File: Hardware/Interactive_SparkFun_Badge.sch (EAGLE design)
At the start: 30 parts, among them J1 AVR_SPI_PRG_6PTH, U1 ATMEGA328P

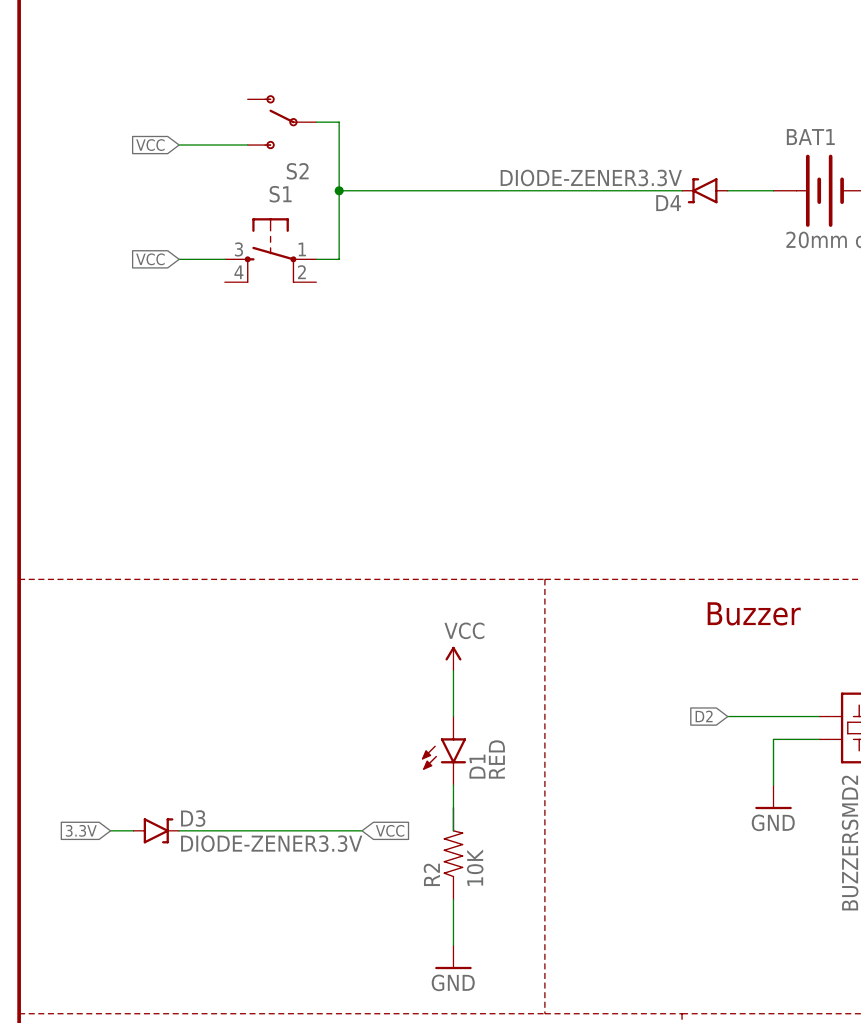
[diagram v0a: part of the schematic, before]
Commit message: Switching to Schottky diode
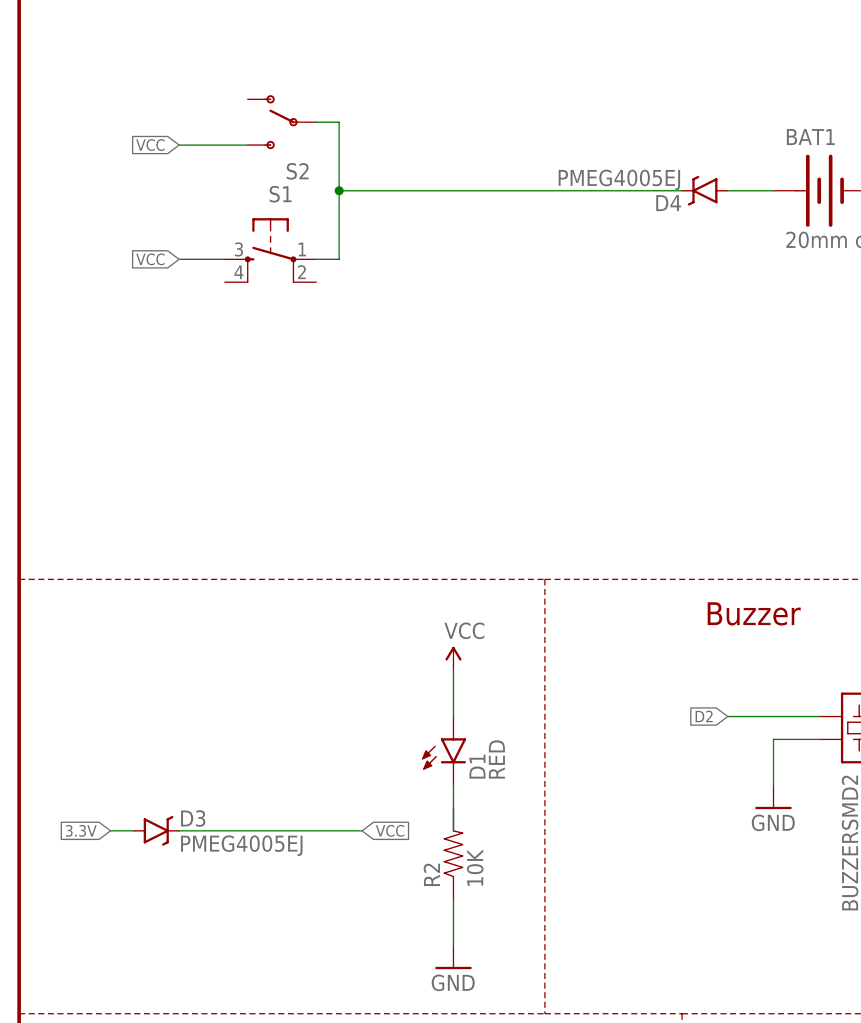
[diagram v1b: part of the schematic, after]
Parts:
- D3, D4: value DIODE-ZENER3.3V -> PMEG4005EJ; device SparkFun-DiscreteSemi:DIODE-ZENER3.3V -> SparkFun-DiscreteSemi:DIODE-SCHOTTKY-PMEG4005EJ
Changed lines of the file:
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@@
 <part name="J1" library="SparkFun-Connectors" deviceset="AVR_SPI_PRG_6" device="PTH" value="AVR_SPI_PRG_6PTH"/>
 <part name="U$3" library="ML8511" deviceset="ALPHABET" device=""/>
-<part name="D3" library="SparkFun-DiscreteSemi" deviceset="DIODE-ZENER" device="3.3V"/>
-<part name="D4" library="SparkFun-DiscreteSemi" deviceset="DIODE-ZENER" device="3.3V"/>
+<part name="D3" library="SparkFun-DiscreteSemi" deviceset="DIODE-SCHOTTKY" device="-PMEG4005EJ" value="PMEG4005EJ"/>
+<part name="D4" library="SparkFun-DiscreteSemi" deviceset="DIODE-SCHOTTKY" device="-PMEG4005EJ" value="PMEG4005EJ"/>
 <part name="C1" library="SparkFun-Capacitors" deviceset="0.1UF-25V(+80/-20%)(0603)" device="" value="0.1uF"/>
 <part name="S1" library="SparkFun-Electromechanical" deviceset="TAC_SWITCH" device="SMD"/>
